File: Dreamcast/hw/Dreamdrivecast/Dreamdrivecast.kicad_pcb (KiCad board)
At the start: 2 copper layers, 91.4 x 89.9 mm, 12 parts, among them CN1 Molex_52602_0579, J1 Breakout, J2 POWER, J4 Micro_SD_Card, SW1 Lid

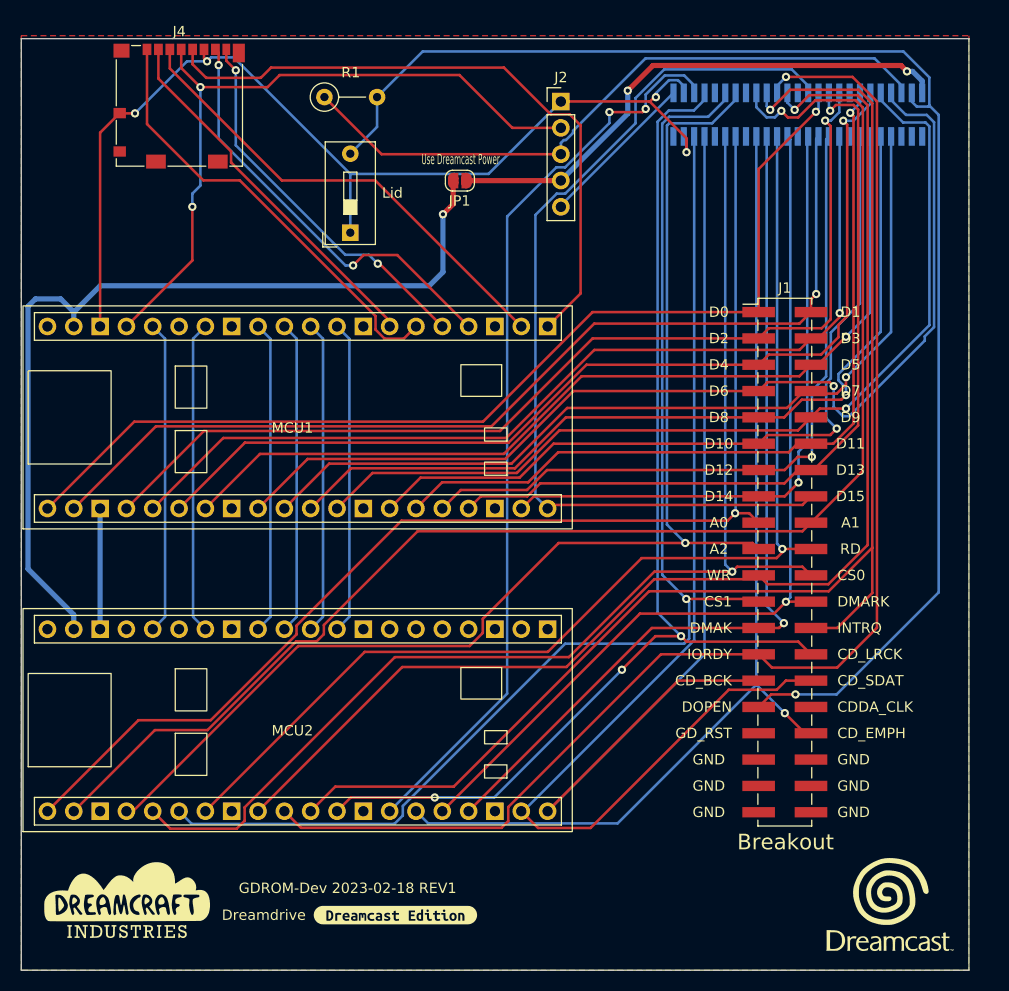
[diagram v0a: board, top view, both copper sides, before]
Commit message: Updated PCB for new schematic design, still needs to be routed.
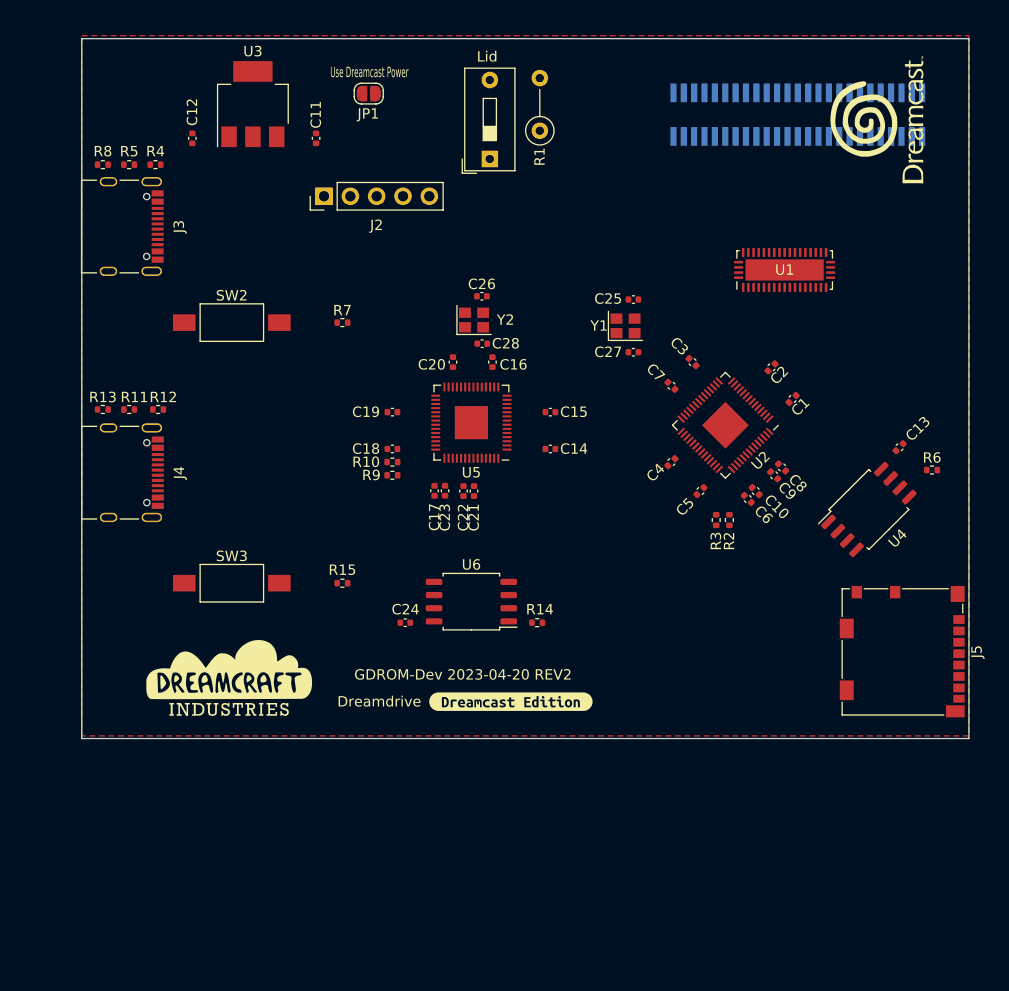
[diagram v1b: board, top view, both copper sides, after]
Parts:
- removed J1: Breakout, Connector_PinHeader_2.54mm:PinHeader_2x20_P2.54mm_Vertical_SMD
- removed MCU1, MCU2: WeAct-RP2040-Pico, WeAct-RP2040-Pico:WeAct-RP2040-Pico
- added C1: 100n, Capacitor_SMD:C_0402_1005Metric, F.Cu at (181.1, 80.8)
- added C10: 1u, Capacitor_SMD:C_0402_1005Metric, F.Cu at (177.5, 89.7)
- added C11: 10u, Capacitor_SMD:C_0402_1005Metric, F.Cu at (135.1, 55.6)
- added C12: 10u, Capacitor_SMD:C_0402_1005Metric, F.Cu at (123.2, 55.6)
- added C13: 100n, Capacitor_SMD:C_0402_1005Metric, F.Cu at (191.4, 85.4)
- added C14: 100n, Capacitor_SMD:C_0402_1005Metric, F.Cu at (157.7, 85.6)
- added C15: 100n, Capacitor_SMD:C_0402_1005Metric, F.Cu at (157.7, 82.0)
- added C16: 100n, Capacitor_SMD:C_0402_1005Metric, F.Cu at (152.1, 77.2)
- added C17: 100n, Capacitor_SMD:C_0402_1005Metric, F.Cu at (146.6, 89.6)
- added C18: 100n, Capacitor_SMD:C_0402_1005Metric, F.Cu at (142.5, 85.6)
- added C19: 100n, Capacitor_SMD:C_0402_1005Metric, F.Cu at (142.5, 82.0)
- added C2: 100n, Capacitor_SMD:C_0402_1005Metric, F.Cu at (179.1, 77.7)
- added C20: 100n, Capacitor_SMD:C_0402_1005Metric, F.Cu at (148.3, 77.2)
- added C21: 100n, Capacitor_SMD:C_0402_1005Metric, F.Cu at (150.4, 89.7)
- added C22: 1u, Capacitor_SMD:C_0402_1005Metric, F.Cu at (149.4, 89.7)
- added C23: 1u, Capacitor_SMD:C_0402_1005Metric, F.Cu at (147.6, 89.6)
- added C24: 100n, Capacitor_SMD:C_0402_1005Metric, F.Cu at (143.7, 102.4)
- added C25: 12p, Capacitor_SMD:C_0402_1005Metric, F.Cu at (165.7, 71.2)
- added C26: 12p, Capacitor_SMD:C_0402_1005Metric, F.Cu at (151.1, 70.9)
- added C27: 12p, Capacitor_SMD:C_0402_1005Metric, F.Cu at (165.7, 76.3)
- added C28: 12p, Capacitor_SMD:C_0402_1005Metric, F.Cu at (151.2, 75.4)
- added C3: 100n, Capacitor_SMD:C_0402_1005Metric, F.Cu at (171.4, 77.2)
- added C4: 100n, Capacitor_SMD:C_0402_1005Metric, F.Cu at (169.4, 86.9)
- added C5: 100n, Capacitor_SMD:C_0402_1005Metric, F.Cu at (172.2, 89.7)
- added C6: 100n, Capacitor_SMD:C_0402_1005Metric, F.Cu at (176.8, 90.4)
- added C7: 100n, Capacitor_SMD:C_0402_1005Metric, F.Cu at (169.4, 79.5)
- added C8: 100n, Capacitor_SMD:C_0402_1005Metric, F.Cu at (180.1, 87.4)
- added C9: 1u, Capacitor_SMD:C_0402_1005Metric, F.Cu at (179.3, 88.1)
- added J3: USB_C_Receptacle_USB2.0, Connector_USB:USB_C_Receptacle_Palconn_UTC16-G, F.Cu at (117.3, 64.1)
- added J5: Micro_SD_Card, Connector_Card:microSD_HC_Molex_104031-0811, F.Cu at (191.7, 105.2)
- added R10: 27.4, Resistor_SMD:R_0402_1005Metric, F.Cu at (142.5, 86.9)
- added R11: 5k1, Resistor_SMD:R_0402_1005Metric, F.Cu at (117.1, 81.8)
- added R12: 5k1, Resistor_SMD:R_0402_1005Metric, F.Cu at (119.9, 81.8)
- added R13: 100k, Resistor_SMD:R_0402_1005Metric, F.Cu at (114.6, 81.8)
- added R14: 10k, Resistor_SMD:R_0402_1005Metric, F.Cu at (156.5, 102.4)
- added R15: 1k, Resistor_SMD:R_0402_1005Metric, F.Cu at (137.7, 98.6)
- added R2: 27.4, Resistor_SMD:R_0402_1005Metric, F.Cu at (175.0, 92.5)
- added R3: 27.4, Resistor_SMD:R_0402_1005Metric, F.Cu at (173.7, 92.5)
- added R4: 5k1, Resistor_SMD:R_0402_1005Metric, F.Cu at (119.6, 58.2)
- added R5: 5k1, Resistor_SMD:R_0402_1005Metric, F.Cu at (117.1, 58.2)
- added R6: 10k, Resistor_SMD:R_0402_1005Metric, F.Cu at (194.6, 87.6)
- added R7: 1k, Resistor_SMD:R_0402_1005Metric, F.Cu at (137.7, 73.4)
- added R8: 100k, Resistor_SMD:R_0402_1005Metric, F.Cu at (114.6, 58.2)
- added R9: 27.4, Resistor_SMD:R_0402_1005Metric, F.Cu at (142.5, 88.1)
- added SW2: MCU1_BOOT, Button_Switch_SMD:SW_SPST_FSMSM, F.Cu at (127.0, 73.4)
- added SW3: MCU2_BOOT, Button_Switch_SMD:SW_SPST_FSMSM, F.Cu at (127.0, 98.6)
- added U1: TS3L501ERUA, Package_DFN_QFN:WQFN-42-1EP_3.5x9mm_P0.5mm_EP2.05x7.55mm, F.Cu at (180.3, 68.3)
- added U2: RP2040, Package_DFN_QFN:QFN-56-1EP_7x7mm_P0.4mm_EP3.2x3.2mm, F.Cu at (174.6, 83.3)
- added U3: AZ1117-3.3, Package_TO_SOT_SMD:SOT-223, F.Cu at (129.0, 52.3)
- added U4: W25Q128JVS, Package_SO:SOIC-8_5.23x5.23mm_P1.27mm, F.Cu at (188.5, 91.4)
- added U5: RP2040, Package_DFN_QFN:QFN-56-1EP_7x7mm_P0.4mm_EP3.2x3.2mm, F.Cu at (150.1, 83.1)
- added U6: W25Q128JVS, Package_SO:SOIC-8_5.23x5.23mm_P1.27mm, F.Cu at (150.1, 100.3)
- added Y1: 12MHz 10ppm, Crystal:Crystal_SMD_2520-4Pin_2.5x2.0mm, F.Cu at (165.0, 73.7)
- added Y2: 12MHz 10ppm, Crystal:Crystal_SMD_2520-4Pin_2.5x2.0mm, F.Cu at (150.4, 73.2)
- J4: value Micro_SD_Card -> USB_C_Receptacle_USB2.0; footprint Connector_Card:microSD_HC_Molex_104031-0811 -> Connector_USB:USB_C_Receptacle_Palconn_UTC16-G
- moved G*** 75.7 mm to (189.2, 53.8), turned to 90 degrees
- moved J4 35.7 mm to (117.3, 87.9), turned to -90 degrees
- moved J2 24.6 mm to (135.9, 61.2), turned to 90 degrees
- moved G*** 23.6 mm to (126.7, 108.1)
- moved kibuzzard-63F149CE 23.4 mm to (153.9, 110.0)
- moved R1 21.0 mm to (156.7, 54.9), turned to 90 degrees
- moved SW1 15.2 mm to (151.9, 57.6)
- moved JP1 12.2 mm to (140.2, 51.3)
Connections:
- CN1 pad A1: unconnected-(CN1-PadA1) -> /+3V3_DREAMCAST
- CN1 pad A13: unconnected-(CN1-PadA13) -> GND
- CN1 pad A15: /RD -> /MCU1_GPIO16
- CN1 pad A18: unconnected-(CN1-PadA18) -> GND
- CN1 pad A21: unconnected-(CN1-PadA21) -> GND
- CN1 pad A25: unconnected-(CN1-PadA25) -> +12V
- CN1 pad A3: unconnected-(CN1-PadA3) -> +5V
- CN1 pad A8: unconnected-(CN1-PadA8) -> GND
- CN1 pad B1: +3V3 -> /+3V3_DREAMCAST
- CN1 pad B13: unconnected-(CN1-PadB13) -> GND
- CN1 pad B14: /WR -> /MCU1_GPIO17
- CN1 pad B18: unconnected-(CN1-PadB18) -> GND
- CN1 pad B21: unconnected-(CN1-PadB21) -> GND
- CN1 pad B8: unconnected-(CN1-PadB8) -> GND
- JP1 pad 1: /PICO_VSYS -> VBUS
- JP1 pad 2: +3V3 -> /+3V3_DREAMCAST
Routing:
- net /A1: track 138.9 -> 0.00 mm, vias 1 -> 0
- net /DOPEN: track 137.5 -> 0.00 mm, vias 1 -> 0
- net /INTRQ: track 132.2 -> 0.00 mm, vias 1 -> 0
- net /IORDY: track 130.1 -> 0.00 mm, vias 1 -> 0
- net /IDE_CS1: track 123.2 -> 0.00 mm, vias 1 -> 0
- net /WR: track 122.6 -> 0.00 mm, vias 1 -> 0
- net /A2: track 122.1 -> 0.00 mm, vias 1 -> 0
- net /IDE_CS0: track 118.0 -> 0.00 mm, vias 1 -> 0
- net /A0: track 117.8 -> 0.00 mm, vias 1 -> 0
- net GND: track 114.1 -> 0.00 mm, vias 4 -> 0
- net /CD_LRCK: track 110.1 -> 0.00 mm, vias 3 -> 0
- net /RD: track 109.1 -> 0.00 mm, vias 1 -> 0
- net /CD_SDAT: track 106.6 -> 0.00 mm
- net /D6: track 102.1 -> 0.00 mm, vias 1 -> 0
- net /D0: track 100.0 -> 0.00 mm, vias 1 -> 0
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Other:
- board size 91.4 x 89.9 mm -> 85.6 x 67.5 mm
- copper layers 2 -> 4
- board text added: "GDROM-Dev 2023-04-20 REV2"
- board text removed: "A0"
- board text removed: "A1"
- board text removed: "A2"
- board text removed: "CDDA_CLK"
- board text removed: "CD_BCK"
- board text removed: "CD_EMPH"
- board text removed: "CD_LRCK"
- board text removed: "CD_SDAT"
- board text removed: "CS0"
- board text removed: "CS1"
- board text removed: "D0"
- board text removed: "D1"
- board text removed: "D10"
- board text removed: "D11"
- board text removed: "D12"
- board text removed: "D13"
- board text removed: "D14"
- board text removed: "D15"
- board text removed: "D2"
- board text removed: "D3"
- board text removed: "D4"
- board text removed: "D5"
- board text removed: "D6"
- board text removed: "D7"
- board text removed: "D8"
- board text removed: "D9"
- board text removed: "DMAK"
- board text removed: "DMARK"
- board text removed: "DOPEN"
- board text removed: "GDROM-Dev 2023-02-18 REV1"
- board text removed: "GD_RST"
- board text removed: "GND"
- board text removed: "INTRQ"
- board text removed: "IORDY"
- board text removed: "RD"
- board text removed: "WR"

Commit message: Updated pcb for new schematic.
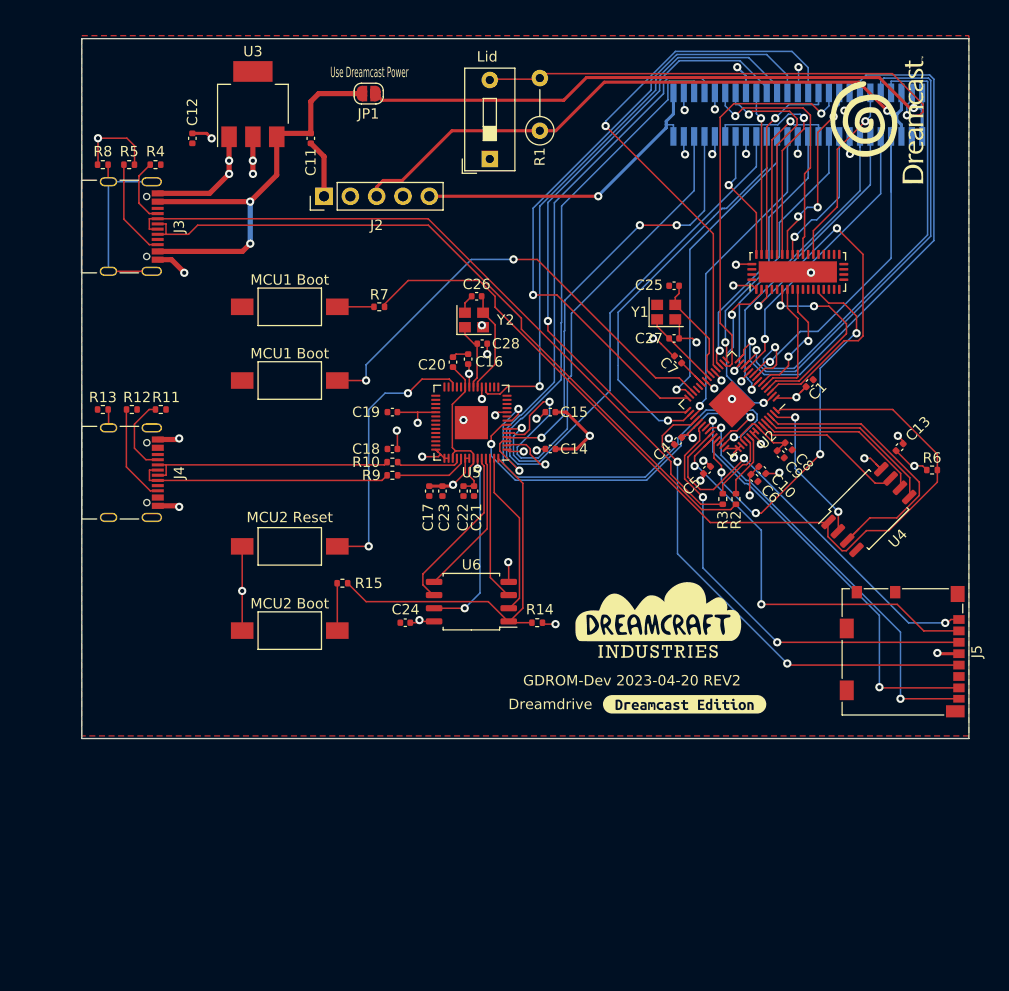
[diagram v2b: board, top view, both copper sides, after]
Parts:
- removed C2, C3: 100n, Capacitor_SMD:C_0402_1005Metric
- added MCU1 Boot: MCU1_BOOT, Button_Switch_SMD:SW_SPST_FSMSM, F.Cu at (132.6, 79.0)
- added MCU2 Reset: MCU1_BOOT, Button_Switch_SMD:SW_SPST_FSMSM, F.Cu at (132.6, 95.0)
- MCU1 Boot: renamed from SW2
- MCU2 Boot: renamed from SW3
- kibuzzard-63F149CE: value G*** -> DDR_DREAMCAST
- moved DREAMCRAFT_LOGO 41.8 mm to (168.1, 102.5)
- moved kibuzzard-63F149CE 16.8 mm to (170.7, 110.2)
- moved MCU2 Boot 7.22 mm to (132.6, 103.1)
- moved MCU1 Boot 5.79 mm to (132.6, 71.9)
- moved C25 4.14 mm to (169.7, 69.8)
- moved C27 4.14 mm to (169.7, 74.9)
- moved Y1 4.14 mm to (168.9, 72.4)
- moved R7 3.87 mm to (141.2, 71.9)
- moved R11 3.05 mm to (120.1, 81.8)
- moved C7 2.62 mm to (170.1, 77.0)
- moved R12 2.54 mm to (117.3, 81.8)
- moved C16 2.36 mm to (149.8, 76.9)
- moved C1 2.25 mm to (182.8, 79.2)
- moved C10 2.13 mm to (178.2, 87.6)
- moved C5 2.13 mm to (172.8, 87.6)
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- renumbered G*** to DREAMCRAFT_LOGO
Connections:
- net /MCU1_GPIO28 renamed /COMMS_PIO_0
- net /MCU1_GPIO29 renamed /COMMS_PIO_1
- CN1 pad A20: /IDE_CS0 -> /CS0
- CN1 pad B20: /IDE_CS1 -> /CS1
- J5 pad 4: /PICO_3v3_OUT -> +3V3
- U1 pad 14: +3V3 -> (no net)
- U1 pad 21: +3V3 -> (no net)
- U1 pad 29: /MUX_CS1 -> /CS1
- U1 pad 30: +3V3 -> (no net)
- U1 pad 33: /MUX_CS0 -> /CS0
- U1 pad 4: +3V3 -> (no net)
- U1 pad 5: GND -> (no net)
- U1 pad 8: +3V3 -> (no net)
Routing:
- net GND: track 0.00 -> 95.7 mm, vias 0 -> 32
- net /MCU1_QSPI_SS: track 0.00 -> 90.0 mm
- net /MCU1_USB_D+: track 0.00 -> 70.2 mm
- net /MCU1_USB_D-: track 0.00 -> 69.3 mm
- net +3V3: track 0.00 -> 65.5 mm, vias 0 -> 27
- net +5V: track 0.00 -> 61.7 mm, vias 0 -> 1
- net /MCU1_GPIO17: track 0.00 -> 61.2 mm, vias 0 -> 1
- net /+3V3_DREAMCAST: track 0.00 -> 59.3 mm, vias 0 -> 1
- net /INTRQ: track 0.00 -> 58.5 mm, vias 0 -> 1
- net /CD_CLK: track 0.00 -> 54.8 mm, vias 0 -> 1
- net /IORDY: track 0.00 -> 54.7 mm, vias 0 -> 1
- net /CD_LRCK: track 0.00 -> 54.4 mm, vias 0 -> 1
- net /D15: track 0.00 -> 54.0 mm, vias 0 -> 1
- net /D11: track 0.00 -> 53.0 mm, vias 0 -> 1
- net /CD_SDAT: track 0.00 -> 52.0 mm, vias 0 -> 1
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- added copper zone on In2.Cu, net +3V3
- added copper zone on In1.Cu, net GND

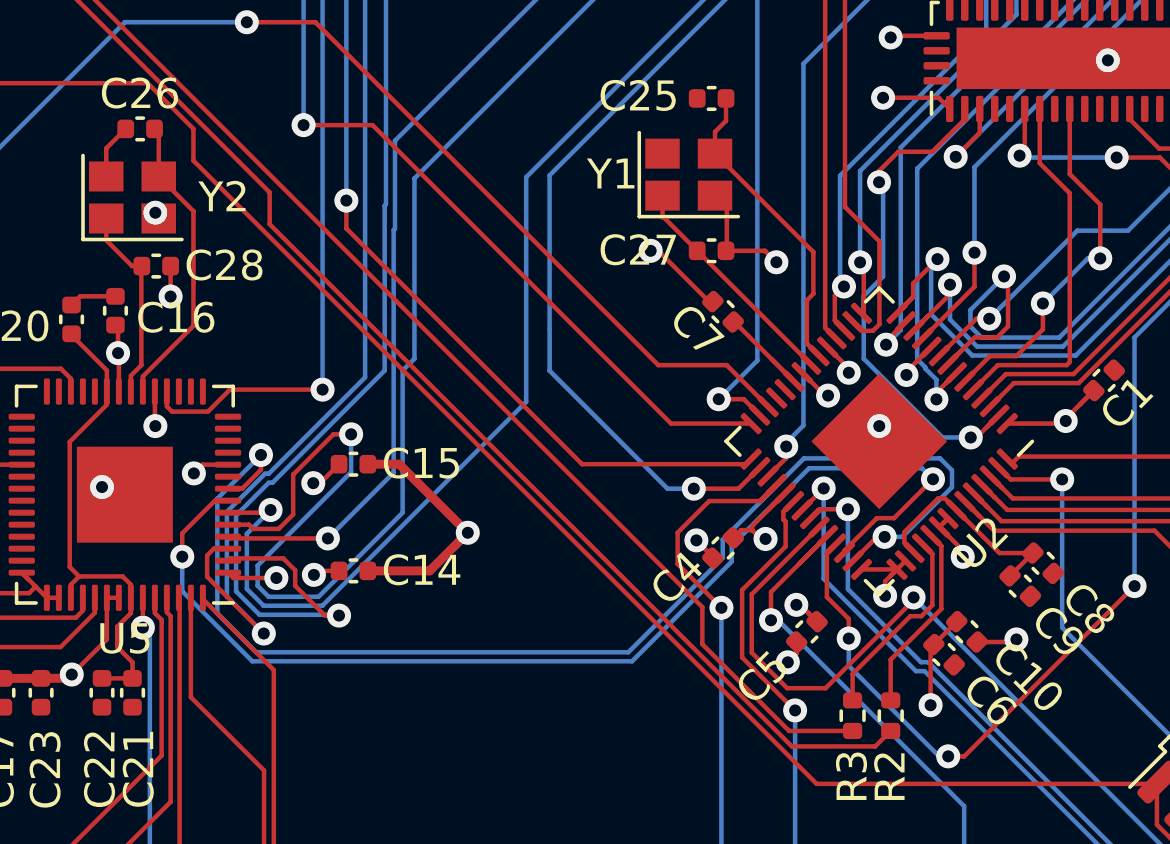
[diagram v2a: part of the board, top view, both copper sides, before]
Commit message: Generated BOM and position files for pcb assembly.
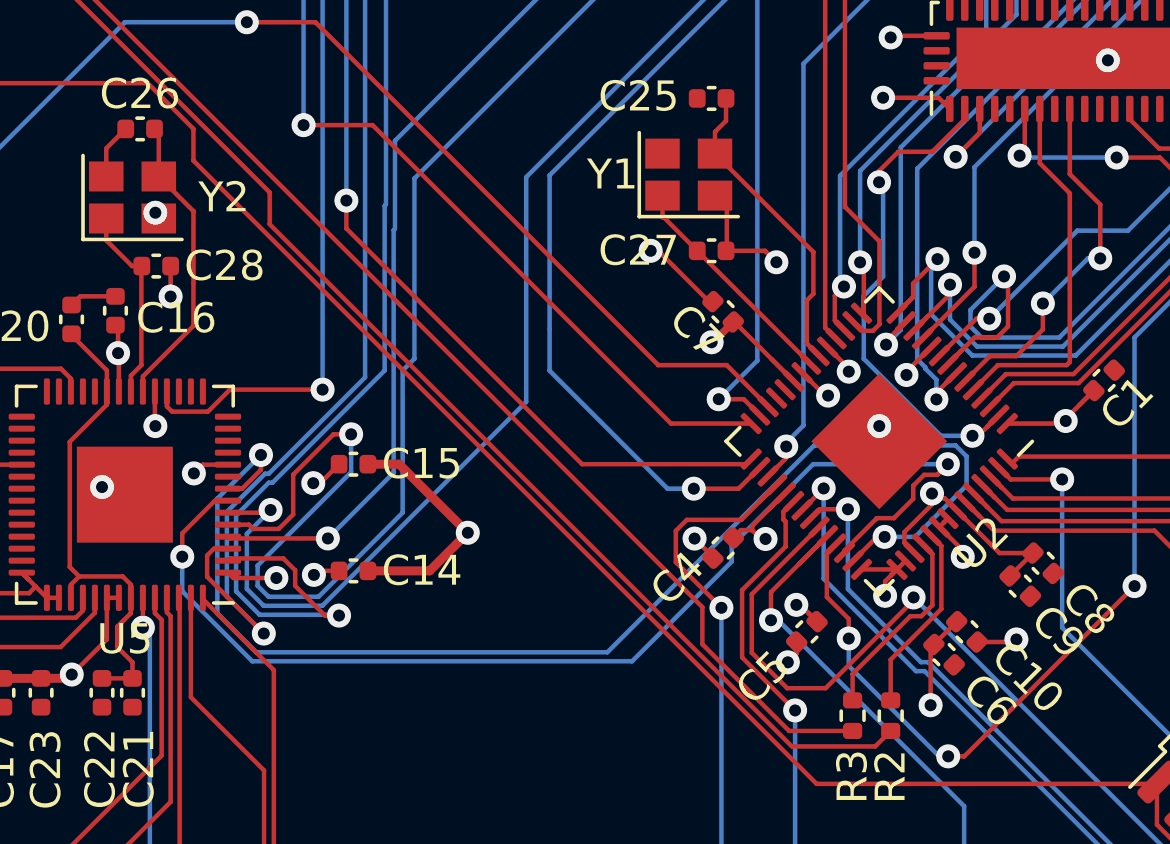
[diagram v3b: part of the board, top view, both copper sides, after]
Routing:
- net +3V3: track 65.5 -> 357.4 mm
- net +1V1: track 28.0 -> 38.7 mm, vias 0 -> 2
- net /COMMS_PIO_0: track 37.1 -> 38.4 mm
- net /COMMS_PIO_1: track 40.8 -> 42.1 mm
- added copper zone on In2.Cu, net (none)
- removed copper zone on In2.Cu, net +3V3

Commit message: Moved some things around. Wrote a struct to contain all the databus pio programs, should make it easier to swap out the cs detect for read/write detect programs. Still not sure how fast that actually is though. Updated BOM for circuit board as well as added part numbers for all populated parts, so checking that in so my hard work doesn't blow away in the wind. Moved databus pio programs (e.g. cs detect) to "sega_databus" in the "shared" directory. There are a few items that need to be updated but at least this compiles for now.
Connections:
- J5 pad 4: +3V3 -> /PICO_3v3_OUT
- U1 pad 14: (no net) -> +3V3
- U1 pad 21: (no net) -> +3V3
- U1 pad 30: (no net) -> +3V3
- U1 pad 4: (no net) -> +3V3
- U1 pad 5: (no net) -> GND
- U1 pad 8: (no net) -> +3V3
